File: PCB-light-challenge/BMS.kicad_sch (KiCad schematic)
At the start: 5 parts, among them U2 AP9101CK, U3 SP8K32FRATB

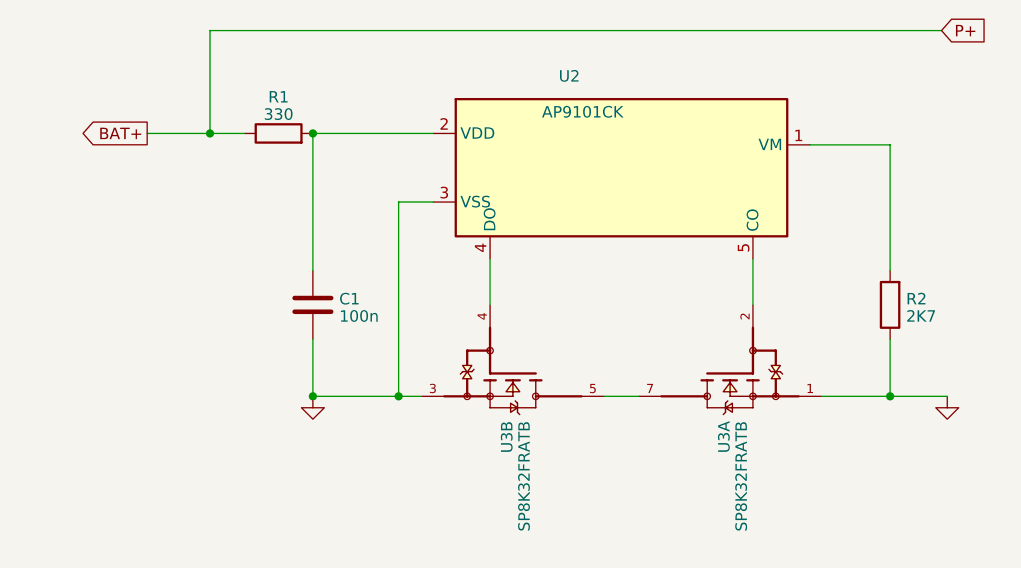
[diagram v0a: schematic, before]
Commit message: TP footprint verandert,  apparte grond (P-) gemaakt.  AC  clearance verandert.  connector voor PIR verandert
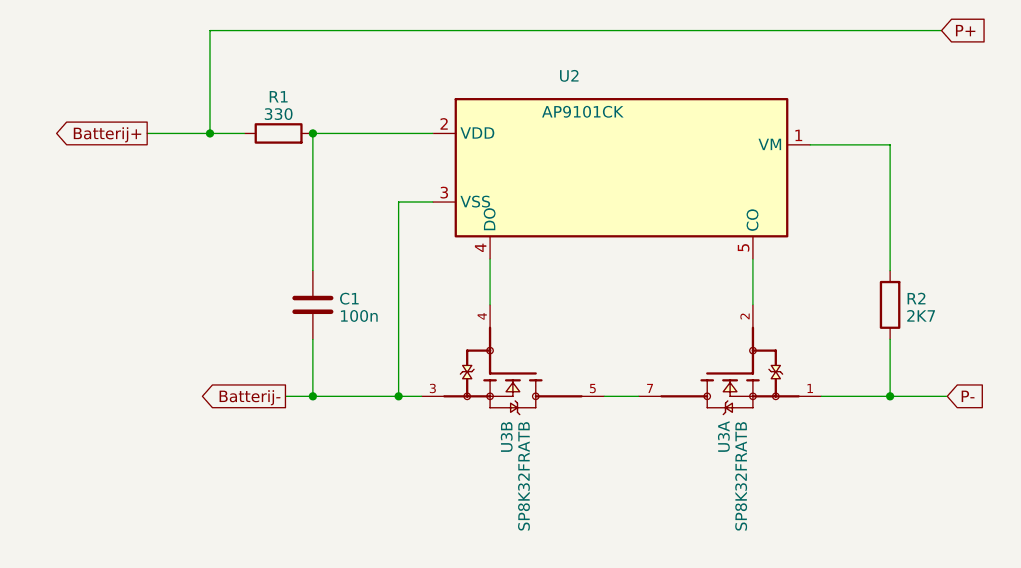
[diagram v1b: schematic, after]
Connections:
- net BAT+ renamed Batterij+
- net GND renamed Batterij-
- net Batterij-: no longer R2.1, U3.1
- new net P-: R2.1, U3.1
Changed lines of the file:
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@@
     (stroke (width 0) (type default))
   )
-  (wire (pts (xy 74.295 74.295) (xy 83.82 74.295))
+  (wire (pts (xy 71.247 74.295) (xy 74.295 74.295))
     (stroke (width 0) (type default))
   )
@@
   )
   (wire (pts (xy 62.865 33.655) (xy 144.145 33.655))
+    (stroke (width 0) (type default))
+  )
+  (wire (pts (xy 74.295 74.295) (xy 83.82 74.295))
     (stroke (width 0) (type default))
   )
@@
     (stroke (width 0) (type default))
   )
+  (global_label "P-" (shape input) (at 144.78 74.295 0) (fields_autoplaced)
+    (effects (font (size 1.27 1.27)) (justify left))
+    (property "Intersheetrefs" "${INTERSHEET_REFS}" (at 150.5282 74.295 0)
+      (effects (font (size 1.27 1.27)) (justify left) hide)
+    )
+  )
   (global_label "P+" (shape input) (at 144.145 33.655 0) (fields_autoplaced)
     (effects (font (size 1.27 1.27)) (justify left))
@@
     )
   )
-  (global_label "BAT+" (shape output) (at 55.88 45.085 180) (fields_autoplaced)
+  (global_label "Batterij+" (shape output) (at 55.88 45.085 180) (fields_autoplaced)
     (effects (font (size 1.27 1.27)) (justify right))
-    (property "Intersheetrefs" "${INTERSHEET_REFS}" (at 48.0756 45.085 0)
+    (property "Intersheetrefs" "${INTERSHEET_REFS}" (at 44.447 45.085 0)
       (effects (font (size 1.27 1.27)) (justify right) hide)
     )
   )
-  (symbol (lib_id "power:GND") (at 144.78 74.295 0) (unit 1)
-    (in_bom yes) (on_board yes) (dnp no) (fields_autoplaced)
-    (property "Reference" "#PWR020" (at 144.78 80.645 0)
-      (effects (font (size 1.27 1.27)) hide)
-    )
-    (property "Value" "GND" (at 144.78 78.4305 0)
-      (effects (font (size 1.27 1.27)) hide)
-    )
-    (property "Footprint" "" (at 144.78 74.295 0)
-      (effects (font (size 1.27 1.27)) hide)
-    )
-    (property "Datasheet" "" (at 144.78 74.295 0)
-      (effects (font (size 1.27 1.27)) hide)
-    )
-    (pin "1")
-    (instances
-      (project "PCB-light-challenge"
-        (path "/35573e8f-7834-430c-81d2-239f316c7834/91ce53e5-ea08-4091-9289-d2f38a19ddbc"
-          (reference "#PWR020") (unit 1)
-        )
-      )
+  (global_label "Batterij-" (shape output) (at 71.247 74.295 180) (fields_autoplaced)
+    (effects (font (size 1.27 1.27)) (justify right))
+    (property "Intersheetrefs" "${INTERSHEET_REFS}" (at 59.814 74.295 0)
+      (effects (font (size 1.27 1.27)) (justify right) hide)
     )
   )
-  (symbol (lib_id "power:GND") (at 74.295 74.295 0) (unit 1)
-    (in_bom yes) (on_board yes) (dnp no) (fields_autoplaced)
-    (property "Reference" "#PWR01" (at 74.295 80.645 0)
-      (effects (font (size 1.27 1.27)) hide)
-    )
-    (property "Value" "GND" (at 74.295 78.4305 0)
-      (effects (font (size 1.27 1.27)) hide)
-    )
-    (property "Footprint" "" (at 74.295 74.295 0)
-      (effects (font (size 1.27 1.27)) hide)
-    )
-    (property "Datasheet" "" (at 74.295 74.295 0)
-      (effects (font (size 1.27 1.27)) hide)
-    )
-    (pin "1")
-    (instances
-      (project "PCB-light-challenge"
-        (path "/35573e8f-7834-430c-81d2-239f316c7834/91ce53e5-ea08-4091-9289-d2f38a19ddbc"
-          (reference "#PWR01") (unit 1)
-        )
-      )
-    )
-  )
